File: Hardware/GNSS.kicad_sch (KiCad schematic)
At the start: 39 parts, among them J1 U.FL, J6 microSD, Q3 BSS138, U2 mosaic-X5

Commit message: More WIP
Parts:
- removed J1: U.FL, SparkFun-Connector:U.FL, symbol SparkFun-RF:U.FL
- removed Q3: BSS138, SparkFun-Semiconductor-Standard:SOT23-3, symbol SparkFun-DiscreteSemi:Q_NMOS_0.2A_50V
- removed R12, R13: 2.2k, SparkFun-Resistor:R_0402_1005Metric, symbol SparkFun-Resistor:2.2k_0402
- removed R16, R41: 169k, SparkFun-Resistor:R_0603_1608Metric, symbol SparkFun-Resistor:169k_0603
- removed TP6: PTH, SparkFun-Connector:1x01, symbol SparkFun-Connector:TestPoint_PTH
- added J1: SMA_Edge, SparkFun-Connector:SMA_Edge, symbol SparkFun-RF:SMA_EdgeMount
- added TP14, TP15, TP18, TP19: PTH, SparkFun-Connector:1x01, symbol SparkFun-Connector:TestPoint_PTH
- D1: value TVS_0402 -> PESD0402
- R5: footprint SparkFun-Resistor:R_0402_1005Metric -> SparkFun-Resistor:R_0603_1608Metric; symbol SparkFun-Resistor:10k_0402 -> SparkFun-Resistor:10k_0603; PROD_ID RES-14241 -> RES-00824
- TP10: renamed from ESP25/MRX4; value 1.0mm -> PTH; footprint SparkFun-Connector:TestPoint-1.0mm -> SparkFun-Connector:1x01; symbol SparkFun-Connector:TestPoint_1.0mm -> SparkFun-Connector:TestPoint_PTH
- TP11: renamed from ESP4/MTX4; value 1.0mm -> PTH; footprint SparkFun-Connector:TestPoint-1.0mm -> SparkFun-Connector:1x01; symbol SparkFun-Connector:TestPoint_1.0mm -> SparkFun-Connector:TestPoint_PTH
- TP12: renamed from ESP14/MRX1; value 1.0mm -> PTH; footprint SparkFun-Connector:TestPoint-1.0mm -> SparkFun-Connector:1x01; symbol SparkFun-Connector:TestPoint_1.0mm -> SparkFun-Connector:TestPoint_PTH
- TP13: renamed from ESP13/MTX1; value 1.0mm -> PTH; footprint SparkFun-Connector:TestPoint-1.0mm -> SparkFun-Connector:1x01; symbol SparkFun-Connector:TestPoint_1.0mm -> SparkFun-Connector:TestPoint_PTH
- TP16: renamed from MRX3; value 1.0mm -> PTH; footprint SparkFun-Connector:TestPoint-1.0mm -> SparkFun-Connector:1x01; symbol SparkFun-Connector:TestPoint_1.0mm -> SparkFun-Connector:TestPoint_PTH
- TP17: renamed from MTX3; value 1.0mm -> PTH; footprint SparkFun-Connector:TestPoint-1.0mm -> SparkFun-Connector:1x01; symbol SparkFun-Connector:TestPoint_1.0mm -> SparkFun-Connector:TestPoint_PTH
- TP20: renamed from MGPIO1; value 1.0mm -> PTH; footprint SparkFun-Connector:TestPoint-1.0mm -> SparkFun-Connector:1x01; symbol SparkFun-Connector:TestPoint_1.0mm -> SparkFun-Connector:TestPoint_PTH
- TP21: renamed from MGPIO2; value 1.0mm -> PTH; footprint SparkFun-Connector:TestPoint-1.0mm -> SparkFun-Connector:1x01; symbol SparkFun-Connector:TestPoint_1.0mm -> SparkFun-Connector:TestPoint_PTH
- renumbered TP_1V8 to TP22
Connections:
- net GND: now also J1.2 (Ext)
- net MOSAIC_RF_IN: now also J1.1 (In)
- net MEventA_1V8: now reaches U2.AC6 (EVENTA)
- net MEventB_1V8: now reaches U2.AC7 (EVENTB)
- net ESP27/MRTS1: now reaches U2.C1 (COM1_RTS)
- net ESP27/MRTS1: now also TP14.1
- net ESP26/MCTS1: now reaches U2.E1 (COM1_CTS)
- net ESP26/MCTS1: now also TP15.1
- net at U2.L1 (COM3_RTS): now also TP18.1
- net at U2.N1 (COM3_CTS): now also TP19.1
- net MPPS renamed MPPS_1V8
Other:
- note removed: "1.8V Inputs protected by 169k/200k divider"
- note removed: "1.8V Output, requires level-shifting"
- note removed: "PPS Level-Shifting"
- moved on the sheet: C24, C28, C30, C31, D7, J6, R27, R28, R29, R30, R31, R32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

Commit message: More WIP
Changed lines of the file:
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@@
+		)
+	)
+	(text "I/O Screw Terminals\n(via level-shifters)"
+		(exclude_from_sim no)
+		(at 115.57 101.6 0)
+		(effects
+			(font
+				(size 1.27 1.27)
+			)
+			(justify left bottom)
 		)
 	)

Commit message: More WIP
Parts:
- added C47: 10uF, SparkFun-Capacitor:C_0603_1608Metric, symbol SparkFun-Capacitor:10uF_0603_10V_20%
- added C48: 0.1uF, SparkFun-Capacitor:C_0603_1608Metric, symbol SparkFun-Capacitor:0.1uF_0603_25V_20%
- added JP14: ~, SparkFun-Jumper:Jumper_3_NC-2_Trace, symbol SparkFun-Jumper:SolderJumper_3_Bridged123
- added R46, R47: 2.2k, SparkFun-Resistor:R_0402_1005Metric, symbol SparkFun-Resistor:2.2k_0402
- added U13: SiT5358AI-FS033IT-10.000000, SparkFun-Semiconductor-Standard:Ceramic_QFN_5.0x3.2mm-10, symbol SparkFun-Clock:SiT5358_TCXO_10MHz_5.0x3.2mm
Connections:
- net 10MHz: now also U13.6 (CLK); no longer C24.1, R30.1, R30.2, R31.1, R32.1, R32.2, U2.AC17 (REF_IN)
- net 3.3V_P: now also C47.1, C48.1, JP14.2 (C), U13.1 (OE), U13.9 (VDD)
- net GND: now also C47.2, C48.2, U13.4 (GND), U13.5 (A0)
- new net: JP14.3 (B), R46.1
- new net: JP14.1 (A), R47.1
- new net: C24.1, R30.1, R32.1
- new net 10MHz_M: R32.2
- new net ESP18/SDA2: R46.2, U13.10 (SDA)
- new net ESP19/SCL2: R47.2, U13.2 (SCL)
- new net REF_IN: R30.2, R31.1, U2.AC17 (REF_IN)
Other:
- note added: "10MHz"
- note added: "10MHz Oscillator"
- note added: "50MHz"
- note added: "50Ohm"

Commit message: Schematic complete
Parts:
- removed C24: 33pF, SparkFun-Capacitor:C_0603_1608Metric, symbol SparkFun-Capacitor:33pF_0603_50V_5%
- removed R30, R31: 1k, SparkFun-Resistor:R_0603_1608Metric, symbol SparkFun-Resistor:1k_0603
- removed R32: 33, SparkFun-Resistor:R_0603_1608Metric, symbol SparkFun-Resistor:33_0603
- added R51: 0, SparkFun-Resistor:R_0603_1608Metric, symbol SparkFun-Resistor:0_0603
- added TP27, TP28, TP29, TP30, TP31, TP32, TP33: PTH, SparkFun-Connector:1x01, symbol SparkFun-Connector:TestPoint_PTH
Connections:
- net 10MHz: now also R51.1, TP33.1; no longer U13.6 (CLK)
- net 3.3V_P: now also TP29.1, TP31.1
- net ESP18/SDA2: now also TP28.1
- net ESP19/SCL2: now also TP27.1
- net GND: now also TP30.1, TP32.1
- new net: R51.2, U13.6 (CLK)
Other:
- note removed: "Clock Shaping"
- note removed: "Divide near module"
- note removed: "Remove harmonics close to source"
- moved on the sheet: C28, C30, C31, C47, C48, D1, D7, J1, J6, JP14, R27, R28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

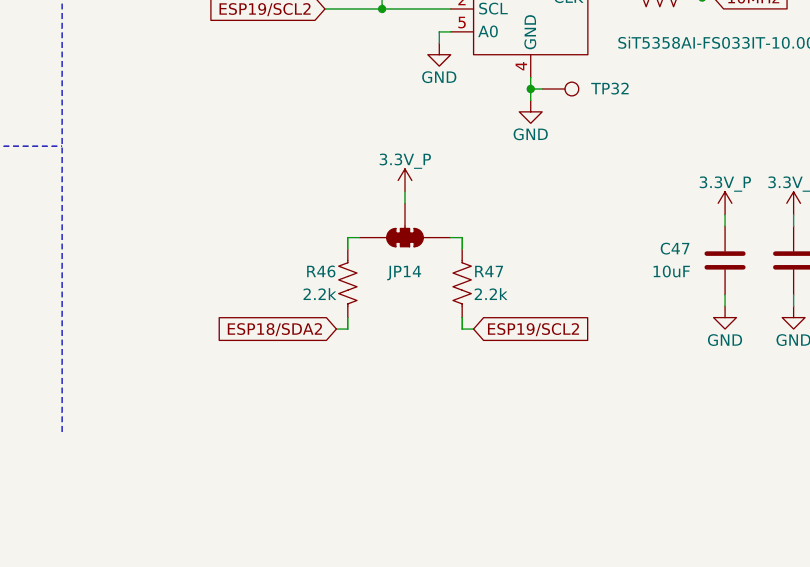
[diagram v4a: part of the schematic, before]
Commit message: Ready for airwire review
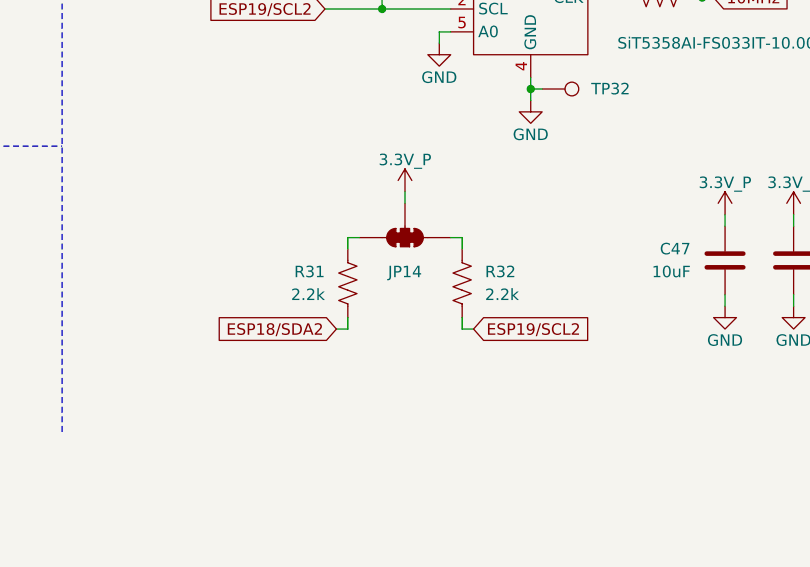
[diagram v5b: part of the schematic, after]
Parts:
- removed R46, R47: 2.2k, SparkFun-Resistor:R_0402_1005Metric, symbol SparkFun-Resistor:2.2k_0402
- added R31, R32: 2.2k, SparkFun-Resistor:R_0603_1608Metric, symbol SparkFun-Resistor:2.2k_0603
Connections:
- net ESP18/SDA2: now also R31.2
- net ESP19/SCL2: now also R32.2
- net at JP14.3 (B): now also R31.1
- net at JP14.1 (A): now also R32.1
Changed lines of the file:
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@@
-	)
-	(symbol
-		(lib_id "SparkFun-Resistor:2.2k_0402")
-		(at 191.77 154.94 270)
-		(mirror x)
-		(unit 1)
-		(exclude_from_sim no)
-		(in_bom yes)
-		(on_board yes)
-		(dnp no)
-		(property "Reference" "R46"
-			(at 190.5 153.67 90)
-			(effects
-				(font
-					(size 1.27 1.27)
-				)
-				(justify right)
-			)
-		)
-		(property "Value" "2.2k"
-			(at 190.5 156.21 90)
-			(effects
-				(font
-					(size 1.27 1.27)
-				)
-				(justify right)
-			)
-		)
-		(property "Footprint" "SparkFun-Resistor:R_0402_1005Metric"
-			(at 187.452 154.94 0)
-			(effects
-				(font
-					(size 1.27 1.27)
-				)
-				(hide yes)
-			)
-		)
-		(property "Datasheet" "https://www.vishay.com/docs/20035/dcrcwe3.pdf"
-			(at 182.88 154.94 0)
-			(effects
-				(font
-					(size 1.27 1.27)
-				)
-				(hide yes)
-			)
-		)
-		(property "Description" "Resistor"
-			(at 191.77 154.94 0)
-			(effects
-				(font
-					(size 1.27 1.27)
-				)
-				(hide yes)
-			)
-		)
-		(property "PROD_ID" "RES-14341"
-			(at 184.912 154.94 0)
-			(effects
-				(font
-					(size 1.27 1.27)
-				)
-				(hide yes)
-			)
-		)
-		(pin "1"
-		)
-		(pin "2"
-		)
-		(instances
-			(project "SparkFun_RTK_mosaic-T"
-				(path "/e3dd3ae4-244d-4cba-9cca-5d2abf83f29a/1004b21d-c362-4c5d-adad-4952c3ff3811"
-					(reference "R46")
-					(unit 1)
-				)
-			)
-		)
 	)
 	(symbol
@@
 	)
 	(symbol
+		(lib_id "SparkFun-Resistor:2.2k_0603")
+		(at 204.47 154.94 90)
+		(unit 1)
+		(exclude_from_sim no)
+		(in_bom yes)
+		(on_board yes)
+		(dnp no)
+		(fields_autoplaced yes)
+		(property "Reference" "R32"
+			(at 207.01 153.6699 90)
+			(effects
+				(font
+					(size 1.27 1.27)
+				)
+				(justify right)
+			)
+		)
+		(property "Value" "2.2k"
+			(at 207.01 156.2099 90)
+			(effects
+				(font
+					(size 1.27 1.27)
+				)
+				(justify right)
+			)
+		)
+		(property "Footprint" "SparkFun-Resistor:R_0603_1608Metric"
+			(at 208.788 154.94 0)
+			(effects
+				(font
+					(size 1.27 1.27)
+				)
+				(hide yes)
+			)
+		)
+		(property "Datasheet" "https://www.vishay.com/docs/20035/dcrcwe3.pdf"
+			(at 213.36 154.94 0)
+			(effects
+				(font
+					(size 1.27 1.27)
+				)
+				(hide yes)
+			)
+		)
+		(property "Description" "Resistor"
+			(at 215.9 154.94 0)
+			(effects
+				(font
+					(size 1.27 1.27)
+				)
+				(hide yes)
+			)
+		)
+		(property "PROD_ID" "RES-08272"
+			(at 211.328 154.94 0)
+			(effects
+				(font
+					(size 1.27 1.27)
+				)
+				(hide yes)
+			)
+		)
+		(pin "2"
+		)
+		(pin "1"
+		)
+		(instances
+			(project "SparkFun_RTK_mosaic-T"
+				(path "/e3dd3ae4-244d-4cba-9cca-5d2abf83f29a/1004b21d-c362-4c5d-adad-4952c3ff3811"
+					(reference "R32")
+					(unit 1)
+				)
+			)
+		)
+	)
+	(symbol
 		(lib_id "SparkFun-Connector:TestPoint_PTH")
 		(at 99.06 66.04 270)
@@
 	)
 	(symbol
-		(lib_id "SparkFun-Resistor:2.2k_0402")
-		(at 204.47 154.94 90)
-		(unit 1)
-		(exclude_from_sim no)
-		(in_bom yes)
-		(on_board yes)
-		(dnp no)
-		(property "Reference" "R47"
-			(at 205.74 153.67 90)
-			(effects
-				(font
-					(size 1.27 1.27)
-				)
-				(justify right)
+		(lib_id "SparkFun-Resistor:2.2k_0603")
+		(at 191.77 154.94 90)
+		(unit 1)
+		(exclude_from_sim no)
+		(in_bom yes)
+		(on_board yes)
+		(dnp no)
+		(fields_autoplaced yes)
+		(property "Reference" "R31"
+			(at 189.23 153.6699 90)
+			(effects
+				(font
+					(size 1.27 1.27)
+				)
+				(justify left)
 			)
 		)
 		(property "Value" "2.2k"
-			(at 205.74 156.21 90)
-			(effects
-				(font
-					(size 1.27 1.27)
-				)
-				(justify right)
-			)
-		)
-		(property "Footprint" "SparkFun-Resistor:R_0402_1005Metric"
-			(at 208.788 154.94 0)
+			(at 189.23 156.2099 90)
+			(effects
+				(font
+					(size 1.27 1.27)
+				)
+				(justify left)
+			)
+		)
+		(property "Footprint" "SparkFun-Resistor:R_0603_1608Metric"
+			(at 196.088 154.94 0)
 			(effects
 				(font
@@
 		)
 		(property "Datasheet" "https://www.vishay.com/docs/20035/dcrcwe3.pdf"
-			(at 213.36 154.94 0)
+			(at 200.66 154.94 0)
 			(effects
 				(font
@@
 		)
 		(property "Description" "Resistor"
-			(at 204.47 154.94 0)
-			(effects
-				(font
-					(size 1.27 1.27)
-				)
-				(hide yes)
-			)
-		)
-		(property "PROD_ID" "RES-14341"
-			(at 211.328 154.94 0)
-			(effects
-				(font
-					(size 1.27 1.27)
-				)
-				(hide yes)
-			)
-		)
-		(pin "1"
+			(at 203.2 154.94 0)
+			(effects
+				(font
+					(size 1.27 1.27)
+				)
+				(hide yes)
+			)
+		)
+		(property "PROD_ID" "RES-08272"
+			(at 198.628 154.94 0)
+			(effects
+				(font
+					(size 1.27 1.27)
+				)
+				(hide yes)
+			)
 		)
 		(pin "2"
 		)
-		(instances
-			(project "SparkFun_RTK_mosaic-T"
-				(path "/e3dd3ae4-244d-4cba-9cca-5d2abf83f29a/1004b21d-c362-4c5d-adad-4952c3ff3811"
-					(reference "R47")
-					(unit 1)
-				)
+		(pin "1"
+		)
+		(instances
+			(project ""
+				(path "/e3dd3ae4-244d-4cba-9cca-5d2abf83f29a/1004b21d-c362-4c5d-adad-4952c3ff3811"
+					(reference "R31")
+					(unit 1)
+				)

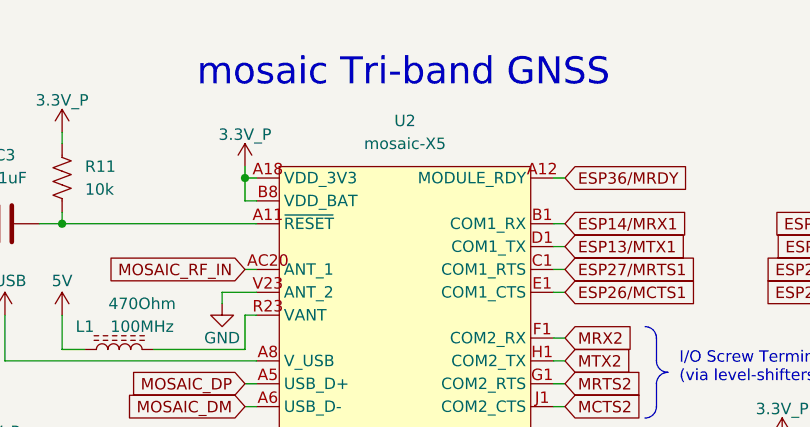
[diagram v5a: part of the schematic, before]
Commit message: Add new PROD_IDs
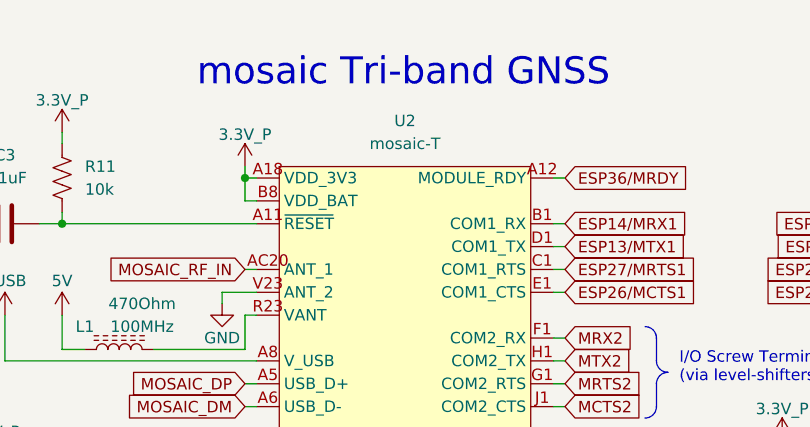
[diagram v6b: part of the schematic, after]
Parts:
- U13: PROD_ID (none) -> XTAL-22764
- U2: value mosaic-X5 -> mosaic-T; symbol SparkFun-GPS:mosaic-X5 -> SparkFun-GPS:mosaic-T; PROD_ID GPS-19395 -> GPS-22762
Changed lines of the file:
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@@
 	)
 	(symbol
-		(lib_id "SparkFun-GPS:mosaic-X5")
+		(lib_id "SparkFun-GPS:mosaic-T")
 		(at 81.28 72.39 0)
 		(unit 1)
@@
 			)
 		)
-		(property "Value" "mosaic-X5"
+		(property "Value" "mosaic-T"
 			(at 81.28 26.67 0)
 			(effects
@@
 			)
 		)
-		(property "Datasheet" "~"
-			(at 68.58 138.43 0)
+		(property "Datasheet" "https://docs.sparkfun.com/SparkFun_RTK_mosaic-X5/assets/component_documentation/Mosaic%20Hardware%20Manual_v1.8.0.pdf"
+			(at 81.28 140.97 0)
 			(effects
 				(font
@@
 		)
 		(property "Description" "Tri-band GNSS receiver"
-			(at 81.28 72.39 0)
-			(effects
-				(font
-					(size 1.27 1.27)
-				)
-				(hide yes)
-			)
-		)
-		(property "PROD_ID" "GPS-19395"
+			(at 81.28 138.43 0)
+			(effects
+				(font
+					(size 1.27 1.27)
+				)
+				(hide yes)
+			)
+		)
+		(property "PROD_ID" "GPS-22762"
 			(at 80.01 135.89 0)
 			(effects
@@
 			)
 		)
-		(property "PROD_ID" ""
+		(property "PROD_ID" "XTAL-22764"
 			(at 212.09 142.24 0)
 			(effects
